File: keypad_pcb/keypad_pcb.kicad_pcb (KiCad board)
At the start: 2 copper layers, 40 x 60 mm, 32 parts, among them U1 KEYPAD_OVERLAY

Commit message: Removing keypad row/column markings from the board
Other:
- board text removed: "C1 C2 C3"
- board text removed: "C4 C5 C6"
- board text removed: "R5 R4 R3 R2 R1"
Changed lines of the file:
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@@
     (area 148.424999 104.924999 188.575001 165.075001)
     (thickness 1.6)
-    (drawings 27)
+    (drawings 24)
     (tracks 405)
     (zones 0)
@@
     (effects (font (size 1.5 1.5) (thickness 0.3)) (justify mirror))
   )
-  (gr_text "R5\nR4\nR3\nR2\nR1" (at 184.6 148.4) (layer F.SilkS)
-    (effects (font (size 1.3 1.2) (thickness 0.25)))
-  )
-  (gr_text "C4\nC5\nC6" (at 153.2 157.2) (layer F.SilkS)
-    (effects (font (size 1.3 1.2) (thickness 0.25)))
-  )
-  (gr_text "C1\nC2\nC3" (at 153.2 133) (layer F.SilkS)
-    (effects (font (size 1.3 1.2) (thickness 0.25)))
-  )
   (gr_text GPIO (at 182.6 122.8) (layer B.SilkS)

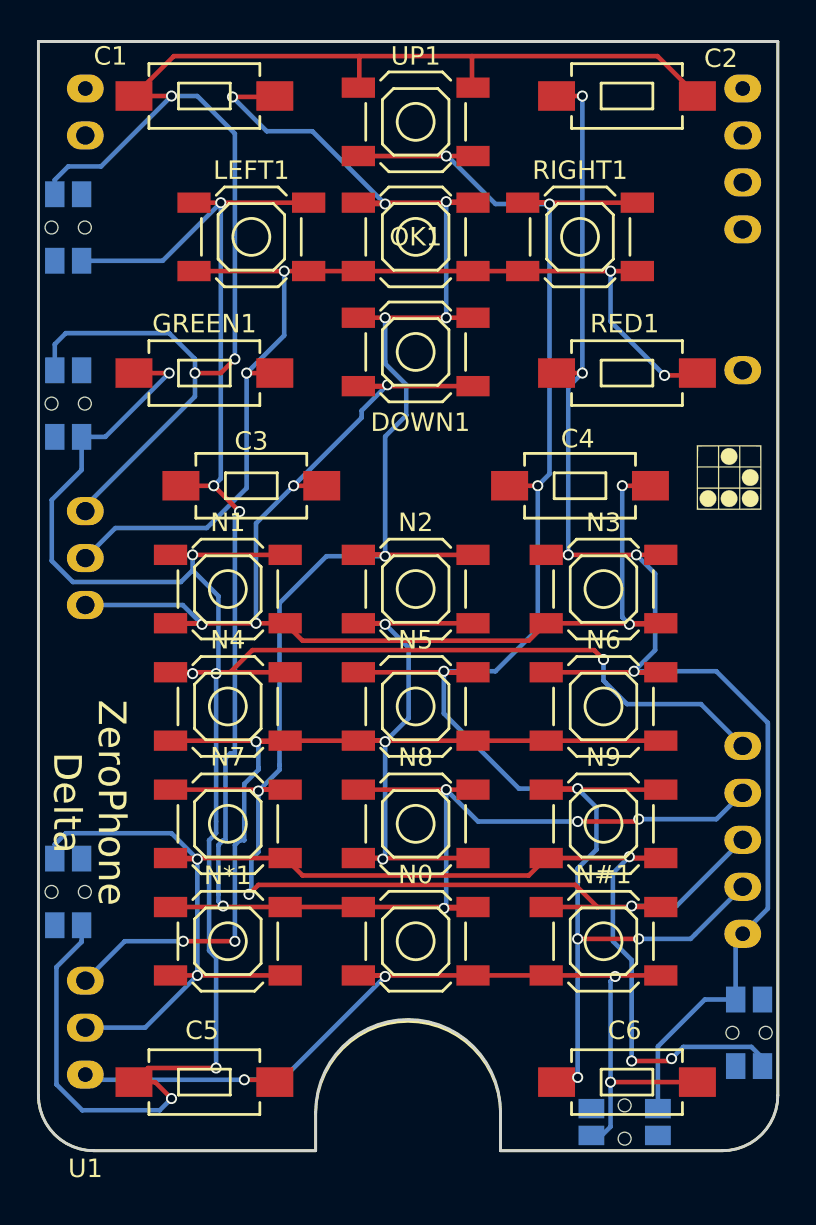
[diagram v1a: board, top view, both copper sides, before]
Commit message: Keypad now has better mechanical strength
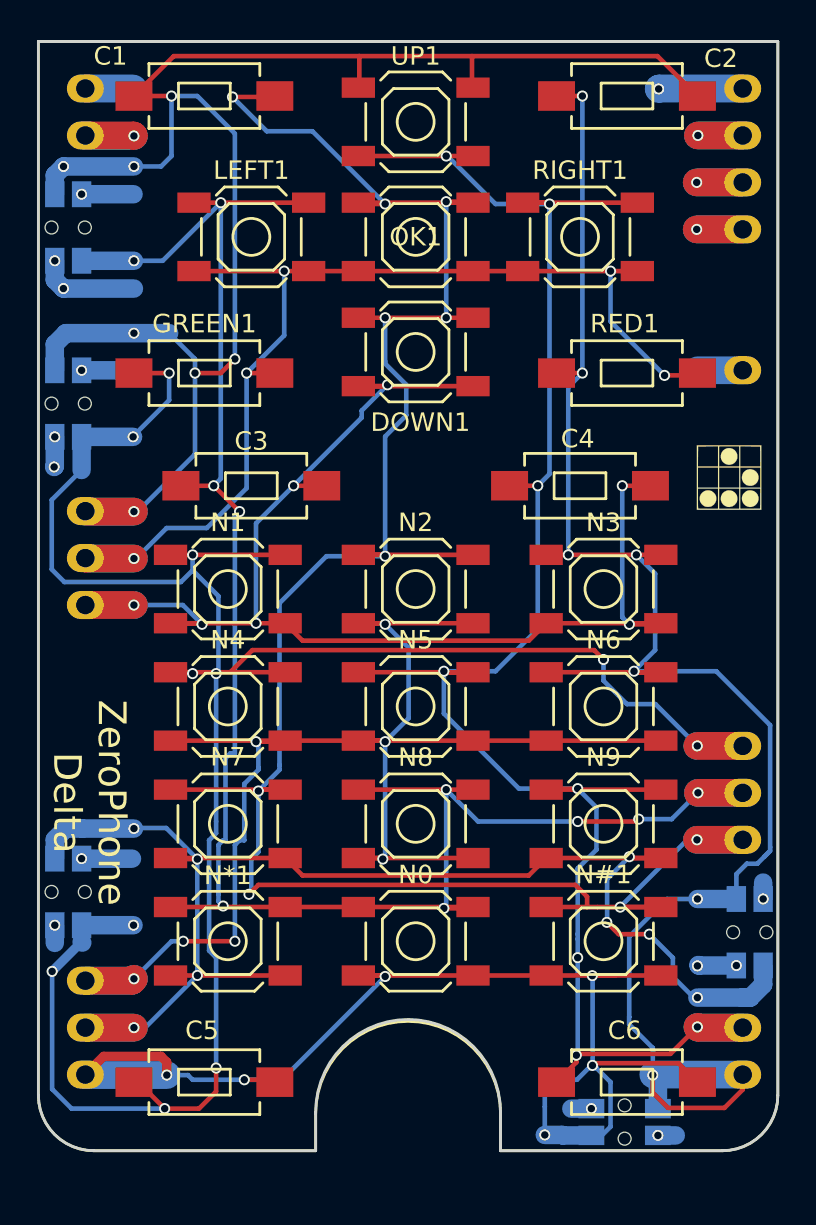
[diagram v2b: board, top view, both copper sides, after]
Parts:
- moved PHOTO1 5.44 mm to (187.0, 153.2)
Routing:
- net (no net): track 0.00 -> 21.5 mm, vias 0 -> 13
- net /COL6: track 52.5 -> 70.2 mm, vias 4 -> 6
- net /ROW1: track 81.7 -> 98.0 mm, vias 5 -> 7
- net /COL1: track 86.2 -> 101.4 mm, vias 3 -> 7
- net /ROW5: track 120.8 -> 129.5 mm, vias 7 -> 11
- net /COL5: track 79.5 -> 87.0 mm, vias 5 -> 8
- net Net-(U1-Pad12): track 0.00 -> 5.28 mm, vias 0 -> 1
- net Net-(U1-Pad17): track 0.00 -> 4.98 mm, vias 0 -> 1
- net Net-(U1-Pad16): track 0.00 -> 4.98 mm, vias 0 -> 1
- net Net-(U1-Pad15): track 0.00 -> 4.85 mm, vias 0 -> 1
- net Net-(U1-Pad14): track 0.00 -> 4.56 mm, vias 0 -> 1
- net /ROW3: track 121.8 -> 125.3 mm, vias 9 -> 10
- net /COL2: track 57.1 -> 60.0 mm, vias 4 -> 5
- net /COL4: track 79.1 -> 81.9 mm, vias 6 -> 7
- net /COL3: track 72.1 -> 74.7 mm, vias 6 -> 7
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
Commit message: Revision label updates, origin points
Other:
- board text added: "ZeroPhone Delta-B"
- board text removed: "ZeroPhone Delta"
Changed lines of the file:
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@@
     (effects (font (size 1.5 1.5) (thickness 0.3)) (justify mirror))
   )
-  (gr_text "ZeroPhone\nDelta" (at 151.257 146.177 270) (layer F.SilkS)
+  (gr_text "ZeroPhone\nDelta-B" (at 151.5 145.4 270) (layer F.SilkS)
     (effects (font (size 1.5 1.5) (thickness 0.3)))
   )
